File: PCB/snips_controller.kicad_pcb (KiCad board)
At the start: 4 copper layers, 35 x 99.9 mm, 85 parts

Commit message: fix: add pull-up on XBee SPI_ATTN pin
SPI_ATTN doubles as the XBee3's BOOTMODE strap; Digi's hardware
reference manual (doc 90001543) says not to let it be tied/pulled low
at reset. R_XBEE_ATTN_PU1 (10kΩ to 3V3) holds it high before firmware
configures the pin, matching the existing R_XBEE_RST1 pull-up pattern
on RESET.

Verified via kicad-cli: the new resistor lands on the XBEE_SPI_ATTN
net alongside U_XBEE1 pin 19 and the MCU's GPIO15, and ERC is clean.

Co-Authored-By: Claude Sonnet 5 <noreply@anthropic.com>
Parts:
- added R_XBEE_ATTN_PU1: 10kΩ, Resistor_SMD:R_0402_1005Metric, F.Cu at (139.6, 147.3)
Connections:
- net /MCU_Core/XBEE_SPI_ATTN renamed /XBee/XBEE_SPI_ATTN
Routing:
- net /XBee/XBEE_SPI_ATTN: track 103.3 -> 105.1 mm
- net 3V3: track 58.1 -> 59.2 mm, vias 10 -> 11

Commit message: fix: swap 3 JLCPCB-out-of-stock parts for in-stock equivalents
C_BAT1/C_BUCK_IN1/C_OLED_1/C_SYS_1/C_VIN_1 (10uF 0805 X5R 16V):
Yageo CC0805KRX5R7BB106 was at 0 stock -> HRE CGA0805X5R106K160MT
(LCSC C6119886, stock ~254k). Identical spec, different brand.

D_VBUS_TVS1: Nexperia PESD5V0S1BA,115 was down to 1 in stock -> TECH
PUBLIC TPPESD5V0S1BA (LCSC C587144, stock ~981k), a widely-stocked
pin/spec-compatible clone of the same part, same SOD-323 package.

Q_PWR1: Diodes Inc DMG2305UX-7 was down to 8 in stock -> Diodes Inc
DMG2305UX-13 (LCSC C144153, stock ~25k) -- same manufacturer, same
part, the -7/-13 suffix is just reel size (7"/13"), not an electrical
variant.

Found via live JLCPCB stock lookups after the JLCPCB upload flagged
these 3 with shortfalls. Verified via kicad-cli sch export bom and
sch erc (0 violations).

Note: PCB/snips_controller.kicad_pcb and the production/ exports still
need another Update-PCB-from-Schematic + Fabrication Toolkit pass to
pick up these changes -- not included here since they're a separate
manual step (see kicad_pcb_sync_gotcha note).

Co-Authored-By: Claude Sonnet 5 <noreply@anthropic.com>
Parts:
- R_ISET1: value 600Ω -> 604Ω

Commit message: task: alert on Basic-library alternatives during JLC part matching (#33)
* task: alert on Basic-library alternatives during JLC part matching

JLC's "Extended" library carries a per-unique-part setup fee on top of
unit price; "Basic" doesn't. That fee doesn't amortize well on a board
with many distinct low-quantity parts -- confirmed the hard way: our
first real JLCPCB assembly quote came back at $333.84 vs PCBWay's
~$190 for the same order, and all 33 of our matched parts were
Extended.

jlc_match.py now does a secondary search for a same-value/same-package
Basic-library part whenever the real match lands on Extended, and
flags it in the report (new BasicAlt column + a Status alert) rather
than silently leaving it. On the current board this surfaces 11
plausible Basic-library swaps (common resistor/cap values, and the
generic 1N4148W diode and 2N7002 MOSFET, which are industry-standard
parts many brands stock identically).

This is alert-only, same as the rest of this script -- it doesn't
touch the schematic. Spot-checked 4 of the 11 suggestions directly
against JLC's catalog to confirm value/package actually match, not
just a keyword hit.

Co-Authored-By: Claude Sonnet 5 <noreply@anthropic.com>

* fix: two correctness bugs in Basic-library alternative matching

1. find_basic_alternative() trusted the raw keyword-search hit without
   verifying the candidate's actual value -- JLC's fuzzy full-text search
   can return a wrong-value part that just shares digits (e.g. searching
   "100 0402" surfaced a 1kΩ resistor, EIA code "1001", as a false match
   for a 100Ω part). Now parses and compares the actual numeric value
   (with unit) before accepting a candidate; falls back to exact
   model-name matching for non-numeric values (generic diode/transistor
   part families like "1N4148W", "2N7002").

2. The new value parser's regex required the unit to be the first
   character of the string, but JLC resistor descriptions carry a
   Chinese prefix ("厚膜电阻 10kΩ ±1%" = "thi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
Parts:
- R_RGB1: value 330Ω -> 470Ω

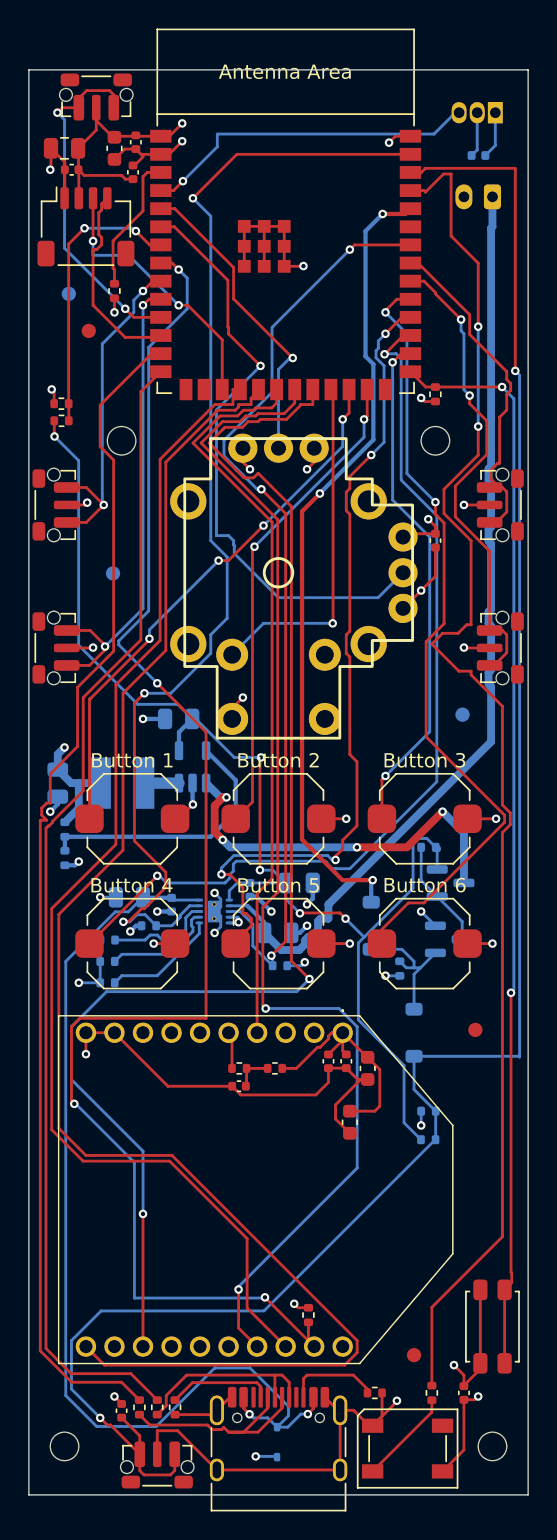
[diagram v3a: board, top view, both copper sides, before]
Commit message: Accelerometer-driven low-power mode (hardware, PCB only) (#47)
* feat: accelerometer-driven low-power mode (hardware, PCB 1/2)

Adds a QMA6100P accelerometer (I2C, shared OLED bus) and enables
host-commanded XBee pin-sleep, laying the hardware groundwork for a
low-power mode: OLED off + XBee sleep after a short idle timeout (no
buttons, no motion), full soft-latch power-off after a longer one.

- QMA6100P chosen after checking JLCPCB's actual parts library: no
  candidate accelerometer is Basic-library, so it won on price, size,
  and standby current (500nA), which matters since it has to watch for
  motion through the whole low-power period.
- Hand-authored symbol + footprint (no existing library part) — pad
  geometry pulled from JLCPCB/LCSC's own EasyEDA component data
  (LCSC C2887190), not estimated from the datasheet's low-res drawing.
- New Accelerometer sheet, wired into the existing I2C bus and into a
  new GPIO46 (INT1) interrupt line so the MCU can light-sleep instead
  of polling for wake conditions.
- XBee DTR moved off its permanent GND tie onto GPIO42 (SLEEP_RQ), so
  firmware can actually request/cancel pin-sleep instead of the radio
  being forced awake at all times.
- Placed, routed, DRC- and ERC-clean.

Firmware (driver, low-power state machine) and production file
generation are follow-up work — this PR is hardware/schematic only.

Co-Authored-By: Claude Sonnet 5 <noreply@anthropic.com>

* feat: accelerometer-driven low-power mode (firmware, PCB 2/2)

Progressive-enhancement low-power mode: idle cascade through
full -> dim OLED -> OLED off -> XBee sleep (each stage independently
timed, capped by a configurable aggressiveness mode), plus an
independent auto-poweroff timer that fires regardless of mode.

- PowerManager (power_management.h/.cpp): pure, unit-tested state
  machine. Takes "did anything happen this tick" and current time,
  reports which tier to be in and a one-shot poweroff flag. No
  capability flags needed for progressive enhancemen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
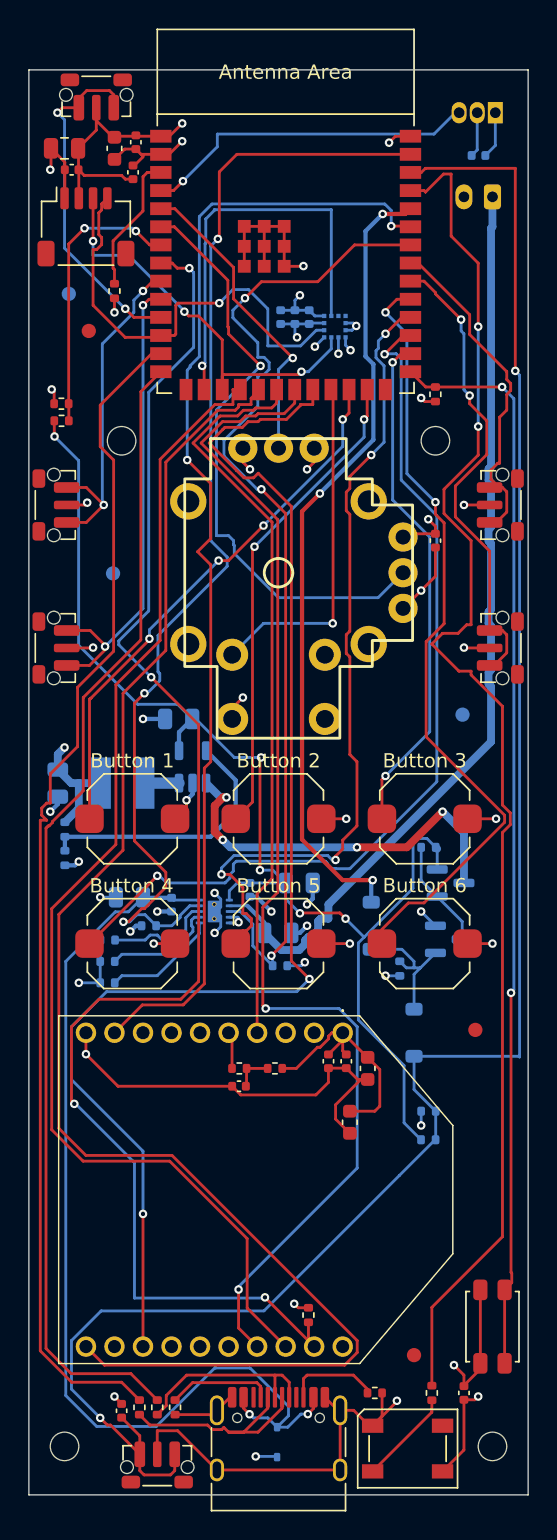
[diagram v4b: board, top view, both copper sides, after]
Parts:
- added C_ACCEL_1: 10nF, Capacitor_SMD:C_0402_1005Metric, B.Cu at (137.7, 77.3)
- added C_ACCEL_2: 100pF, Capacitor_SMD:C_0402_1005Metric, B.Cu at (139.7, 77.3)
- added C_ACCEL_3: 2.2nF, Capacitor_SMD:C_0402_1005Metric, B.Cu at (138.7, 77.3)
- added U_ACCEL1: QMA6100P, SnipsControllers_Custom:QMA6100P, B.Cu at (141.4, 78.0)
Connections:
- net /MCU_Core/I2C_SCL renamed /Accelerometer/I2C_SCL
- net /MCU_Core/I2C_SDA renamed /Accelerometer/I2C_SDA
- U_MCU1 pad 16: unconnected-(U_MCU1-GPIO46-Pad16) -> ACCEL_INT1
- U_MCU1 pad 35: unconnected-(U_MCU1-MTMS/GPIO42-Pad35) -> XBEE_SLEEP_RQ
- U_XBEE1 pad 9: GND -> XBEE_SLEEP_RQ
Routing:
- net XBEE_SLEEP_RQ: track 0.00 -> 80.0 mm, vias 0 -> 2
- net ACCEL_INT1: track 0.00 -> 28.7 mm, vias 0 -> 1
- net /Accelerometer/I2C_SDA: track 14.0 -> 31.6 mm, vias 0 -> 1
- net /Accelerometer/I2C_SCL: track 19.0 -> 29.2 mm, vias 2 -> 3
- net GND: track 164.6 -> 172.3 mm, vias 37 -> 41
- net 3V3: track 59.2 -> 64.3 mm, vias 11 -> 13
- net /MCU_Core/STAT2: track 66.2 -> 71.0 mm
- net /MCU_Core/STAT1: track 81.0 -> 79.1 mm
- net /XBee/XBEE_SPI_ATTN: track 105.1 -> 103.7 mm

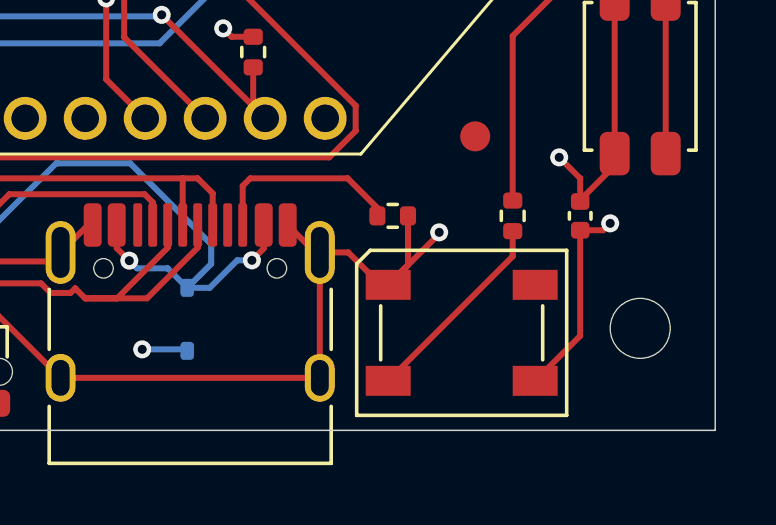
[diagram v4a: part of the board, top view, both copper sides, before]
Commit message: fix: correct SK6812 RGB LED footprint mismatch that failed PCBWay assembly
D_RGB1 was still using a stale generic 5.0x5.0mm PLCC4 footprint left
over from before the design switched to the SK6812MINI-E, which is what
PCBWay's assembly check caught. Added a custom footprint sourced from
the real OPSCO SK6812MINI-E-012 datasheet, pointed the schematic at it,
and reworked the PCB placement/routing to match. DRC clean, 0 unconnected.

Co-Authored-By: Claude Sonnet 5 <noreply@anthropic.com>
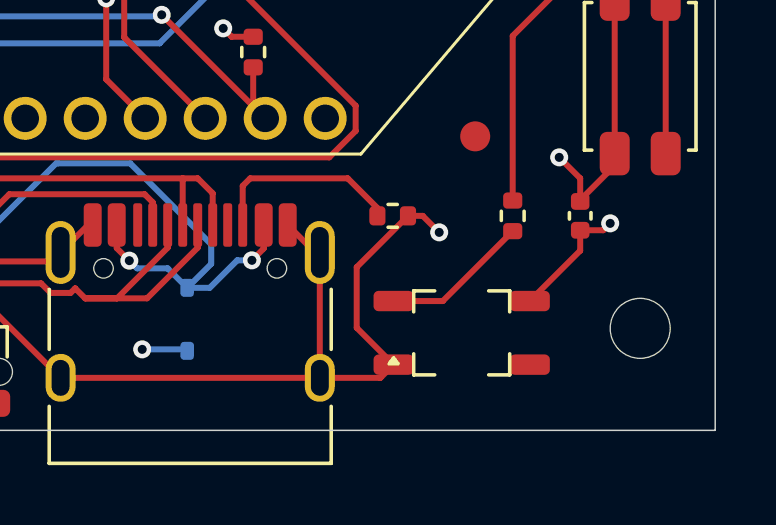
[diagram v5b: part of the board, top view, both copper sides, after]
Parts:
- D_RGB1: value SK6812MINI-E -> SK6812MINI-E-012; footprint LED_SMD:LED_SK6812_PLCC4_5.0x5.0mm_P3.2mm -> SnipsControllers_Custom:SK6812MINI-E-012
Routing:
- net 3V3: track 64.3 -> 61.7 mm
- net GND: track 172.3 -> 174.4 mm
- net /RGB_LED/RGB_DIN_R: track 6.71 -> 4.94 mm

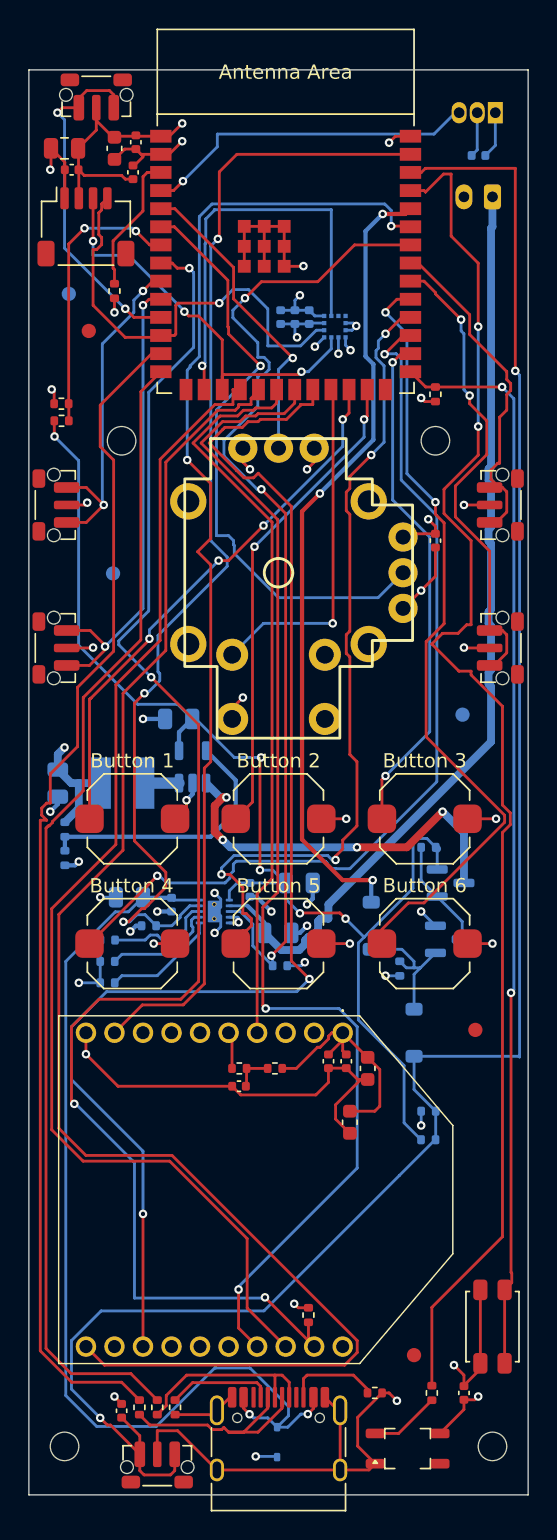
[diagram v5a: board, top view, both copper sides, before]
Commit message: fix: power-latch false-trigger, RGB LED footprint regression, JST connector clarity (#56)
Power latch: battery-only bring-up showed the board powering on immediately
with no button press, because PWR_BTN_SENSE's resistor divider idled at
~VSYS/2, forward-biasing D_OR1's anode directly. Adds a transistor inverter
(R_INV_BASE1 / Q_INV1 / R_INV_PU1) so only an actual button press can
forward-bias D_OR1; removes the now-unnecessary R_PWR_SENSE1. New parts
matched to JLCPCB Basic-library equivalents. PCB layout, diagrams, and
power_control_layout docs updated to match.

RGB LED: fixes a regression where D_RGB1's Footprint had reverted to the
stale large SK6812 PLCC4 part in both the cached lib_symbols default and the
instance override, instead of the custom SK6812MINI-E-012 footprint that
PCBWay's earlier assembly rejection required.

JST battery connector: PCBWay's assembly mounted BT1 vertically instead of
horizontal. Confirmed via two independent distributor sources (JLC + LCSC)
that the specified MPN (S2B-PH-K(LF)(SN)) is genuinely a right-angle/
horizontal part, so this was an assembly-side error, not a design bug.
Made the Value/Description fields explicitly say RIGHT-ANGLE / HORIZONTAL
so it's unambiguous in the exported BOM this time.

Co-authored-by: Claude Sonnet 5 <noreply@anthropic.com>
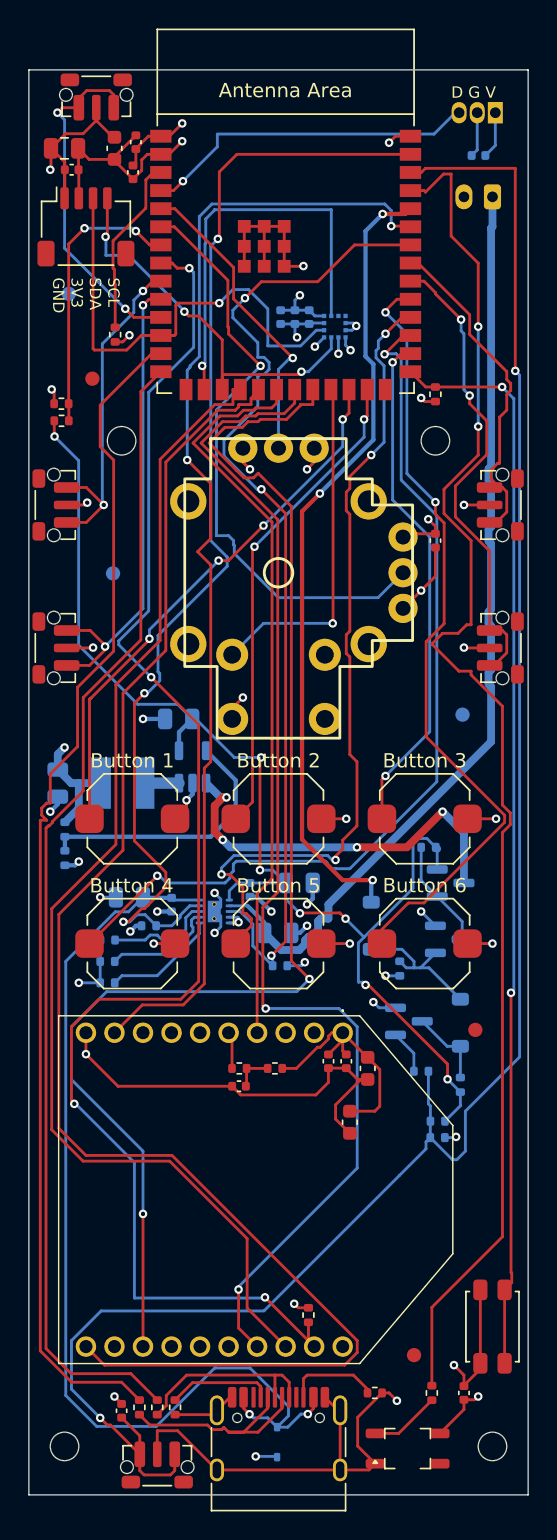
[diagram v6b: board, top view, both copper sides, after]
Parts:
- added Q_INV1: MMBT3904, Package_TO_SOT_SMD:SOT-23, B.Cu at (146.6, 126.7)
- added R_INV_BASE1: 10kΩ, Resistor_SMD:R_0402_1005Metric, B.Cu at (147.5, 130.2)
- added R_INV_PU1: 100kΩ, Resistor_SMD:R_0402_1005Metric, B.Cu at (150.2, 131.2)
- BT1: value JST-PH_2Pin_Battery -> JST-PH_2Pin_Battery_RightAngle_Horizontal
- moved REF** 3.36 mm to (124.5, 81.7)
- moved D_OR1 3.32 mm to (150.2, 126.8)
- moved R_EN_PU1 3.06 mm to (126.0, 78.6)
- moved R_PWR_SENSE1 1.96 mm to (148.7, 134.8), turned to 0 degrees
- moved R_BTN_PU1 1.46 mm to (148.7, 133.7), turned to 180 degrees
- turned C_3V3_2 to -90 degrees
- turned C_3V3_3 to 90 degrees
- turned C_OLED_1 to 180 degrees
- turned C_OLED_2 to 180 degrees
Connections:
- D_OR1 pad 2: /MCU_Core/PWR_BTN_SENSE -> /Power_Control/PWR_BTN_TRIGGER
- U_OLED1 pad 1: 3V3 -> GND
- U_OLED1 pad 2: GND -> 3V3
- U_OLED1 pad 3: /Accelerometer/I2C_SCL -> /Accelerometer/I2C_SDA
- U_OLED1 pad 4: /Accelerometer/I2C_SDA -> /Accelerometer/I2C_SCL
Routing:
- net /Power_Control/PWR_BTN_TRIGGER: track 0.00 -> 5.59 mm
- net 3V3: track 61.7 -> 65.5 mm, vias 13 -> 12
- net /Power_Control/PWR_BTN_INV_BASE: track 0.00 -> 3.08 mm
- net /MCU_Core/MCU_EN: track 9.79 -> 12.6 mm
- net /MCU_Core/PWR_BTN_SENSE: track 132.8 -> 135.2 mm
- net /Accelerometer/I2C_SDA: track 31.6 -> 33.4 mm
- net /Accelerometer/I2C_SCL: track 29.2 -> 28.4 mm
- net /Power_Control/PWR_LATCH_G: track 10.0 -> 10.6 mm
- net GND: track 174.4 -> 173.8 mm, vias 41 -> 43
- net VSYS: track 85.6 -> 86.2 mm, vias 5 -> 7
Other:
- board text added: "D G V"
- board text added: "G"
- board text added: "SCL SDA 3V3 GND"
- board text added: "Snips Controllers V1.1 by @thePunderWoman github.com/thePunderWoman/SnipsControllers"
- board text added: "V"
- board text added: "V G D"
- board text removed: "Snips Controllers V1.0 by @thePunderWoman github.com/thePunderWoman/SnipsControllers"
